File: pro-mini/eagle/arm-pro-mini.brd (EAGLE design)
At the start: 38.1 x 20.3 mm, 61 parts, among them J1 MICRO USB, J2 SWD HEADER, Q1 12Mhz, T1 MMBT3906, U1 PRTR5V0U2X, U2 MIC5225-3.3v, U3 LPC11U35FHI33/501, U4 BAS40-05

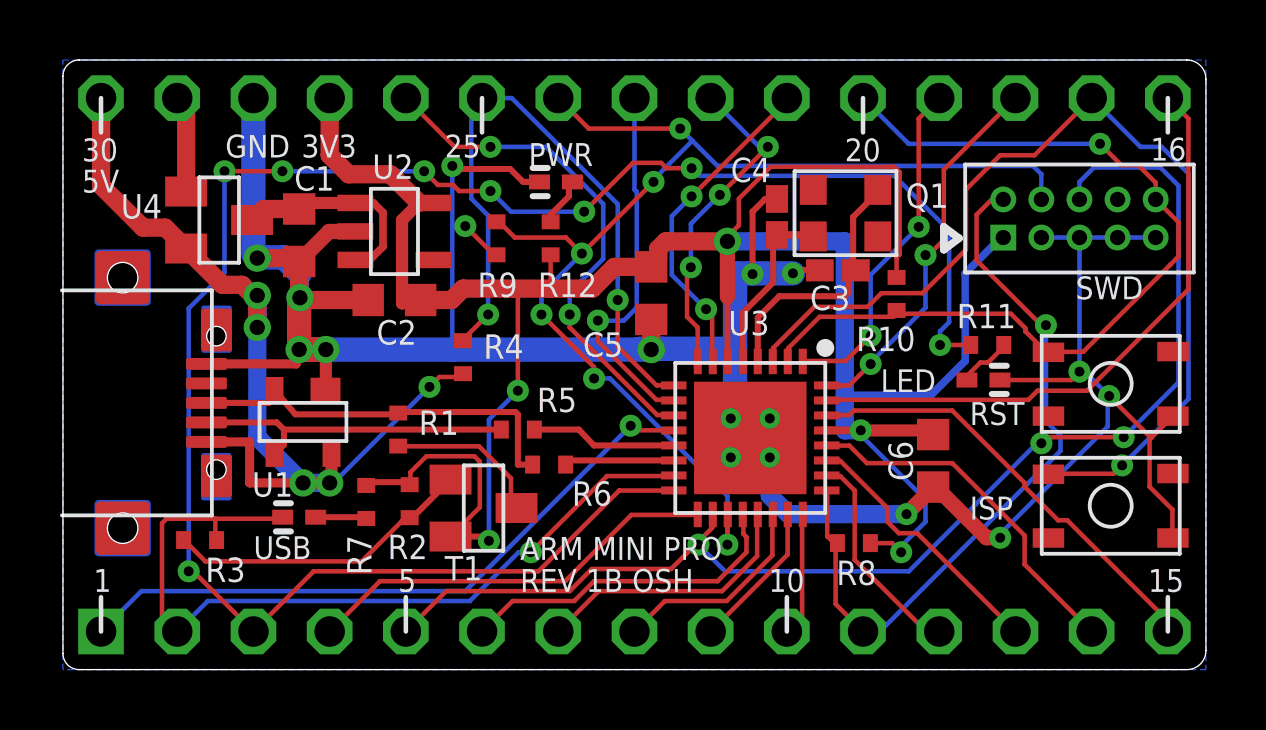
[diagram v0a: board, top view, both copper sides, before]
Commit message: Increased the holes of the SWD header. Improved the polarit markers of the LEDs.
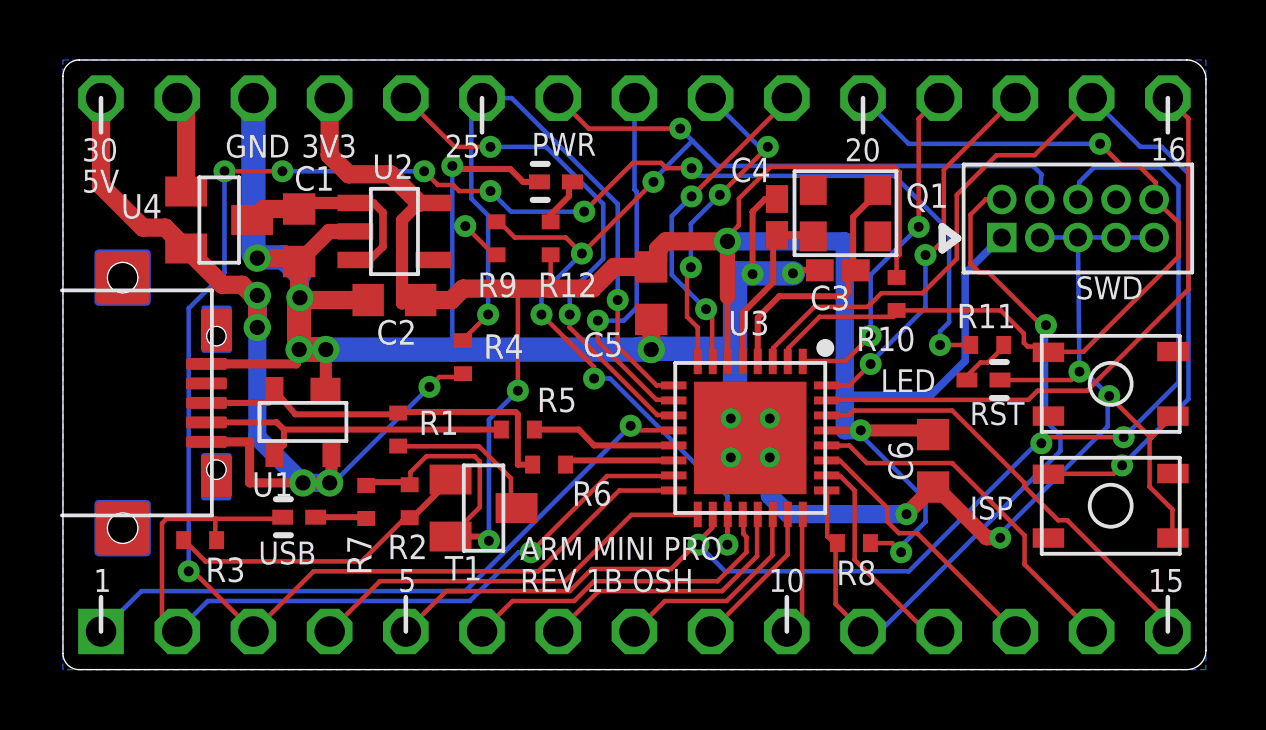
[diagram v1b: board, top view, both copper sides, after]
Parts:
- moved J2 0.05 mm to (33.8, 15.0)
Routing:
- net PIO0_15-SWDIO: track 24.6 -> 25.4 mm
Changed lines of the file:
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@@
 <setting verticaltext="up"/>
 </settings>
-<grid distance="1" unitdist="mil" unit="mil" style="lines" multiple="1" display="yes" altdistance="1" altunitdist="mil" altunit="mil"/>
+<grid distance="0.000123031496" unitdist="mil" unit="mil" style="lines" multiple="1" display="yes" altdistance="1" altunitdist="mil" altunit="mil"/>
 <layers>
 <layer number="1" name="Top" color="4" fill="1" visible="yes" active="yes"/>
@@
 <text x="30.226" y="8.1534" size="0.762" layer="21" font="vector" ratio="10">RST</text>
 <text x="30.226" y="5.0038" size="0.762" layer="21" font="vector" ratio="10">ISP</text>
-<text x="15.5194" y="16.7894" size="0.762" layer="21" font="vector" ratio="10">PWR</text>
+<text x="15.62264375" y="17.128796875" size="0.762" layer="21" font="vector" ratio="10">PWR</text>
 <text x="27.2542" y="9.2456" size="0.762" layer="21" font="vector" ratio="10">LED</text>
-<text x="6.35" y="3.683" size="0.762" layer="21" font="vector" ratio="10">USB</text>
+<text x="6.5122375" y="3.5052" size="0.762" layer="21" font="vector" ratio="10">USB</text>
 <text x="1.016" y="2.5908" size="0.762" layer="21" font="vector" ratio="10">1</text>
 <text x="11.176" y="2.5908" size="0.762" layer="21" font="vector" ratio="10">5</text>
@@
 <param name="mtIsolate" value="1.5mm 0.15mm 0.2mm 0.15mm 0.2mm 0.15mm 0.2mm 0.15mm 0.2mm 0.15mm 0.2mm 0.15mm 0.2mm 0.15mm 0.2mm"/>
 <param name="mdWireWire" value="7mil"/>
-<param name="mdWirePad" value="7mil"/>
+<param name="mdWirePad" value="6mil"/>
 <param name="mdWireVia" value="7mil"/>
-<param name="mdPadPad" value="8mil"/>
+<param name="mdPadPad" value="6mil"/>
 <param name="mdPadVia" value="8mil"/>
 <param name="mdViaVia" value="8mil"/>
@@
 <attribute name="VALUE" x="9.271" y="8.636" size="1.27" layer="27" rot="R270"/>
 </element>
-<element name="J2" library="arm-pro-mini" package="SWD-HEADER" value="SWD HEADER" x="33.8836" y="15.0368" smashed="yes">
-<attribute name="VALUE" x="32.6136" y="10.5918" size="1.27" layer="27"/>
+<element name="J2" library="arm-pro-mini" package="SWD-HEADER" value="SWD HEADER" x="33.8328" y="15.0368" smashed="yes">
+<attribute name="VALUE" x="32.5628" y="10.5918" size="1.27" layer="27"/>
 </element>
 <element name="R8" library="arm-pro-mini" package="R0402" value="10K" x="26.3652" y="4.2164" smashed="yes">
@@
 <wire x1="33.6042" y1="9.652" x2="31.2332" y2="9.652" width="0.1524" layer="1"/>
 <wire x1="33.8836" y1="9.9314" x2="33.6042" y2="9.652" width="0.1524" layer="1"/>
-<wire x1="33.8836" y1="14.4018" x2="33.8836" y2="9.9314" width="0.1524" layer="16"/>
-<wire x1="33.8836" y1="14.4018" x2="32.6136" y2="14.4018" width="0.1524" layer="16"/>
-<wire x1="33.8836" y1="14.4018" x2="35.1536" y2="14.4018" width="0.1524" layer="16"/>
-<wire x1="35.1536" y1="14.4018" x2="36.4236" y2="14.4018" width="0.1524" layer="16"/>
+<wire x1="33.8328" y1="14.4018" x2="33.8836" y2="9.9314" width="0.1524" layer="16"/>
+<wire x1="33.8328" y1="14.4018" x2="32.5628" y2="14.4018" width="0.1524" layer="16"/>
+<wire x1="33.8328" y1="14.4018" x2="35.1028" y2="14.4018" width="0.1524" layer="16"/>
+<wire x1="35.1028" y1="14.4018" x2="36.3728" y2="14.4018" width="0.1524" layer="16"/>
 <wire x1="34.8742" y1="9.1186" x2="36.2712" y2="7.7216" width="0.1524" layer="1"/>
 <wire x1="33.9344" y1="10.0584" x2="34.8742" y2="9.1186" width="0.1524" layer="16"/>
@@
 <wire x1="30.0736" y1="10.287" x2="30.0736" y2="13.208" width="0.254" layer="16"/>
 <wire x1="30.0736" y1="13.208" x2="31.2674" y2="14.4018" width="0.254" layer="16"/>
-<wire x1="31.2674" y1="14.4018" x2="31.3436" y2="14.4018" width="0.254" layer="16"/>
+<wire x1="31.2674" y1="14.4018" x2="31.2928" y2="14.4018" width="0.254" layer="16"/>
 <wire x1="15.1638" y1="9.2964" x2="15.1638" y2="12.573" width="0.1524" layer="1"/>
 <wire x1="15.1638" y1="12.573" x2="15.0368" y2="12.7" width="0.1524" layer="1"/>
@@
 <wire x1="27.7876" y1="11.8618" x2="27.7876" y2="11.9722" width="0.1524" layer="1"/>
 <wire x1="32.766" y1="10.5918" x2="32.8422" y2="10.5918" width="0.1524" layer="1"/>
-<wire x1="32.0802" y1="11.2776" x2="32.766" y2="10.5918" width="0.1524" layer="1"/>
-<wire x1="32.0802" y1="11.3792" x2="32.0802" y2="11.2776" width="0.1524" layer="1"/>
-<wire x1="31.5976" y1="11.8618" x2="32.0802" y2="11.3792" width="0.1524" layer="1"/>
-<wire x1="27.8384" y1="11.8618" x2="31.5976" y2="11.8618" width="0.1524" layer="1"/>
 <wire x1="32.8422" y1="10.5918" x2="32.85" y2="10.575" width="0.1524" layer="1"/>
 <wire x1="27.8384" y1="11.8618" x2="27.7876" y2="11.9722" width="0.1524" layer="1"/>
-<wire x1="34.0106" y1="10.5918" x2="36.9062" y2="13.4874" width="0.1524" layer="1"/>
-<wire x1="36.9062" y1="13.4874" x2="37.1094" y2="13.6906" width="0.1524" layer="1"/>
+<wire x1="34.0106" y1="10.5918" x2="37.1856" y2="13.7668" width="0.1524" layer="1"/>
 <wire x1="32.9184" y1="10.5918" x2="34.0106" y2="10.5918" width="0.1524" layer="1"/>
 <wire x1="32.9184" y1="10.5918" x2="32.85" y2="10.575" width="0.1524" layer="1"/>
@@
 <wire x1="35.2806" y1="16.8148" x2="35.8394" y2="16.8148" width="0.1524" layer="1"/>
 <wire x1="35.8394" y1="16.8148" x2="36.4236" y2="16.2306" width="0.1524" layer="1"/>
-<wire x1="36.4236" y1="16.2306" x2="36.4236" y2="15.6718" width="0.1524" layer="1"/>
-<wire x1="37.1856" y1="14.9098" x2="36.4236" y2="15.6718" width="0.1524" layer="1"/>
+<wire x1="36.4236" y1="16.2306" x2="36.3728" y2="15.6718" width="0.1524" layer="1"/>
+<wire x1="37.1856" y1="14.9098" x2="36.3728" y2="15.6718" width="0.1524" layer="1"/>
 <wire x1="37.1856" y1="14.9098" x2="37.1856" y2="13.7668" width="0.1524" layer="1"/>
-<wire x1="37.1856" y1="13.7668" x2="37.1094" y2="13.6906" width="0.1524" layer="1"/>
+<wire x1="32.766" y1="10.5918" x2="32.5882" y2="10.7696" width="0.1524" layer="1"/>
+<wire x1="32.5882" y1="10.7696" x2="32.1564" y2="10.7696" width="0.1524" layer="1"/>
+<wire x1="32.1564" y1="10.7696" x2="32.0294" y2="10.8966" width="0.1524" layer="1"/>
+<wire x1="32.0294" y1="10.8966" x2="32.0294" y2="11.2014" width="0.1524" layer="1"/>
+<wire x1="32.0294" y1="11.2014" x2="31.2586" y2="11.9722" width="0.1524" layer="1"/>
+<wire x1="31.2586" y1="11.9722" x2="27.7876" y2="11.9722" width="0.1524" layer="1"/>
 </signal>
 <signal name="PIO0_10-SWDCLK">
@@
 <via x="19.685" y="16.256" extent="1-16" drill="0.3302"/>
 <wire x1="32.3342" y1="16.7894" x2="32.6136" y2="16.51" width="0.1524" layer="16"/>
-<wire x1="32.6136" y1="16.51" x2="32.6136" y2="15.6718" width="0.1524" layer="16"/>
+<wire x1="32.6136" y1="16.51" x2="32.5628" y2="15.6718" width="0.1524" layer="16"/>
 </signal>
 <signal name="PIO0_15-SWDIO">
@@
 <wire x1="26.67" y1="1.27" x2="25.7556" y2="2.1844" width="0.1524" layer="1"/>
 <wire x1="25.7556" y1="4.1656" x2="25.8152" y2="4.2164" width="0.1524" layer="1"/>
-<wire x1="32.6136" y1="11.4808" x2="30.4546" y2="13.6398" width="0.1524" layer="1"/>
 <wire x1="32.766" y1="11.4808" x2="32.6136" y2="11.4808" width="0.1524" layer="1"/>
 <wire x1="32.766" y1="8.2804" x2="32.766" y2="11.4808" width="0.1524" layer="16"/>
@@
 <wire x1="26.67" y1="1.27" x2="27.2288" y2="1.27" width="0.1524" layer="16"/>
 <via x="32.766" y="11.4808" extent="1-16" drill="0.3302"/>
-<wire x1="30.4546" y1="13.6398" x2="30.4546" y2="15.1638" width="0.1524" layer="1"/>
-<wire x1="30.4546" y1="15.1638" x2="30.9626" y2="15.6718" width="0.1524" layer="1"/>
-<wire x1="30.9626" y1="15.6718" x2="31.3436" y2="15.6718" width="0.1524" layer="1"/>
+<wire x1="30.9626" y1="15.6718" x2="31.2928" y2="15.6718" width="0.1524" layer="1"/>
+<wire x1="32.6136" y1="11.4808" x2="30.861" y2="13.2334" width="0.1524" layer="1"/>
+<wire x1="30.861" y1="13.2334" x2="30.5562" y2="13.2334" width="0.1524" layer="1"/>
+<wire x1="30.5562" y1="13.2334" x2="30.2514" y2="13.5382" width="0.1524" layer="1"/>
+<wire x1="30.2514" y1="13.5382" x2="30.2514" y2="15.1638" width="0.1524" layer="1"/>
+<wire x1="30.2514" y1="15.1638" x2="30.7594" y2="15.6718" width="0.1524" layer="1"/>
+<wire x1="30.7594" y1="15.6718" x2="31.2928" y2="15.6718" width="0.1524" layer="1"/>
 </signal>
 <signal name="PIO0_1-ISP_EN">
@@
 <wire x1="36.6268" y1="17.4244" x2="35.9156" y2="17.4244" width="0.1524" layer="16"/>
 <wire x1="35.9156" y1="17.4244" x2="34.29" y2="19.05" width="0.1524" layer="16"/>
-<wire x1="28.6512" y1="12.5476" x2="30.099" y2="13.9954" width="0.1524" layer="1"/>
-<wire x1="30.099" y1="13.9954" x2="30.099" y2="16.002" width="0.1524" layer="1"/>
-<wire x1="30.099" y1="16.002" x2="31.242" y2="17.145" width="0.1524" layer="1"/>
-<wire x1="31.242" y1="17.145" x2="32.385" y2="17.145" width="0.1524" layer="1"/>
+<wire x1="31.115" y1="17.145" x2="32.385" y2="17.145" width="0.1524" layer="1"/>
 <wire x1="32.385" y1="17.145" x2="34.29" y2="19.05" width="0.1524" layer="1"/>
+<wire x1="28.6512" y1="12.5476" x2="29.7942" y2="13.6906" width="0.1524" layer="1"/>
+<wire x1="29.7942" y1="13.6906" x2="29.7942" y2="15.8242" width="0.1524" layer="1"/>
+<wire x1="29.7942" y1="15.8242" x2="31.115" y2="17.145" width="0.1524" layer="1"/>
 </signal>
 <signal name="N$4">
@@
 <wire x1="36.576" y1="16.7386" x2="34.3662" y2="16.7386" width="0.1524" layer="16"/>
 <wire x1="34.3662" y1="16.7386" x2="33.8836" y2="16.256" width="0.1524" layer="16"/>
-<wire x1="33.8836" y1="16.256" x2="33.8836" y2="15.6718" width="0.1524" layer="16"/>
+<wire x1="33.8836" y1="16.256" x2="33.8328" y2="15.6718" width="0.1524" layer="16"/>
 </signal>
 </signals>

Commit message: Updatd license note.
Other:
- board text added: "OSH. Share alike and attributions are optional. Commercial use ok."
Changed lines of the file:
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@@
 <text x="7.9502" y="17.0688" size="0.762" layer="21" font="vector" ratio="10">3V3</text>
 <text x="0.635" y="15.9004" size="0.762" layer="21" font="vector" ratio="10">5V</text>
+<text x="7.14989375" y="-9.83480625" size="0.8128" layer="48" font="vector" ratio="10">OSH. Share alike and attributions
+are optional. Commercial use ok.</text>
 </plain>
 <attributes>
@@
 </board>
 </drawing>
+<compatibility>
+<note version="6.3" minversion="6.2.2" severity="warning">
+Since Version 6.2.2 text objects can contain more than one line,
+which will not be processed correctly with this version.
+</note>
+</compatibility>
 </eagle>

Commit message: Changed R4, R11 from 1.5K to 10K. R4 to reduce max current via MCU protection diodes and R11 to make the red LED less bright.
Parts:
- R11, R4: value 1K5 -> 10K
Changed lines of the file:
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@@
 <attribute name="VALUE" x="29.845" y="12.065" size="1.27" layer="27" rot="R270"/>
 </element>
-<element name="R4" library="arm-pro-mini" package="R0402" value="1K5" x="13.335" y="10.414" smashed="yes" rot="R90">
+<element name="R4" library="arm-pro-mini" package="R0402" value="10K" x="13.335" y="10.414" smashed="yes" rot="R90">
 <attribute name="NAME" x="14.0208" y="10.3632" size="0.8128" layer="25" font="vector" ratio="10"/>
 <attribute name="VALUE" x="15.24" y="9.779" size="1.27" layer="27" rot="R90"/>
@@
 <attribute name="VALUE" x="14.351" y="15.0114" size="1.27" layer="27" rot="R270"/>
 </element>
-<element name="R11" library="arm-pro-mini" package="R0402" value="1K5" x="30.8102" y="10.8204" smashed="yes" rot="R180">
+<element name="R11" library="arm-pro-mini" package="R0402" value="10K" x="30.8102" y="10.8204" smashed="yes" rot="R180">
 <attribute name="NAME" x="29.7942" y="11.3792" size="0.8128" layer="25" font="vector" ratio="10"/>
 <attribute name="VALUE" x="31.4452" y="12.7254" size="1.27" layer="27" rot="R180"/>
